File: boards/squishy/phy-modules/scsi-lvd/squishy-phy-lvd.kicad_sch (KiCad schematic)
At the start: 14 parts, among them J1 SCSI PHY Mezz, J2 SCSI Connector, U1 M24C02-RMC

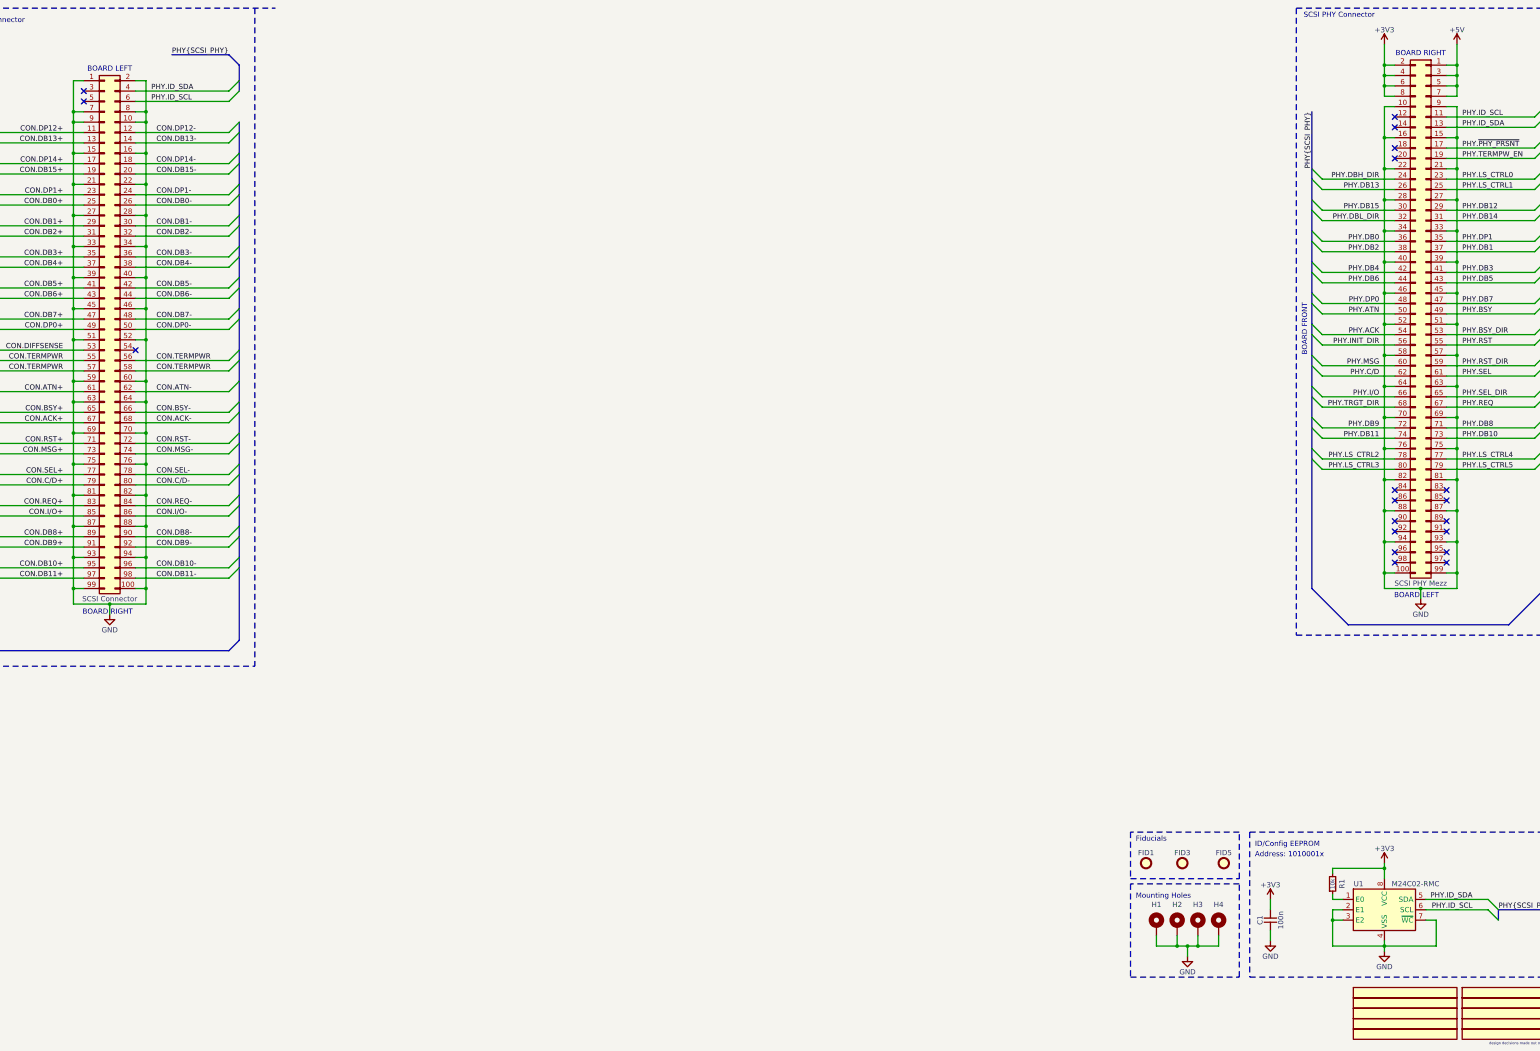
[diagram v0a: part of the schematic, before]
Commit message: squishy: phy: lvd: Large chunk of work on the LVD phy,
still needs diffsense and termpwr bits implemented and then it can be routed
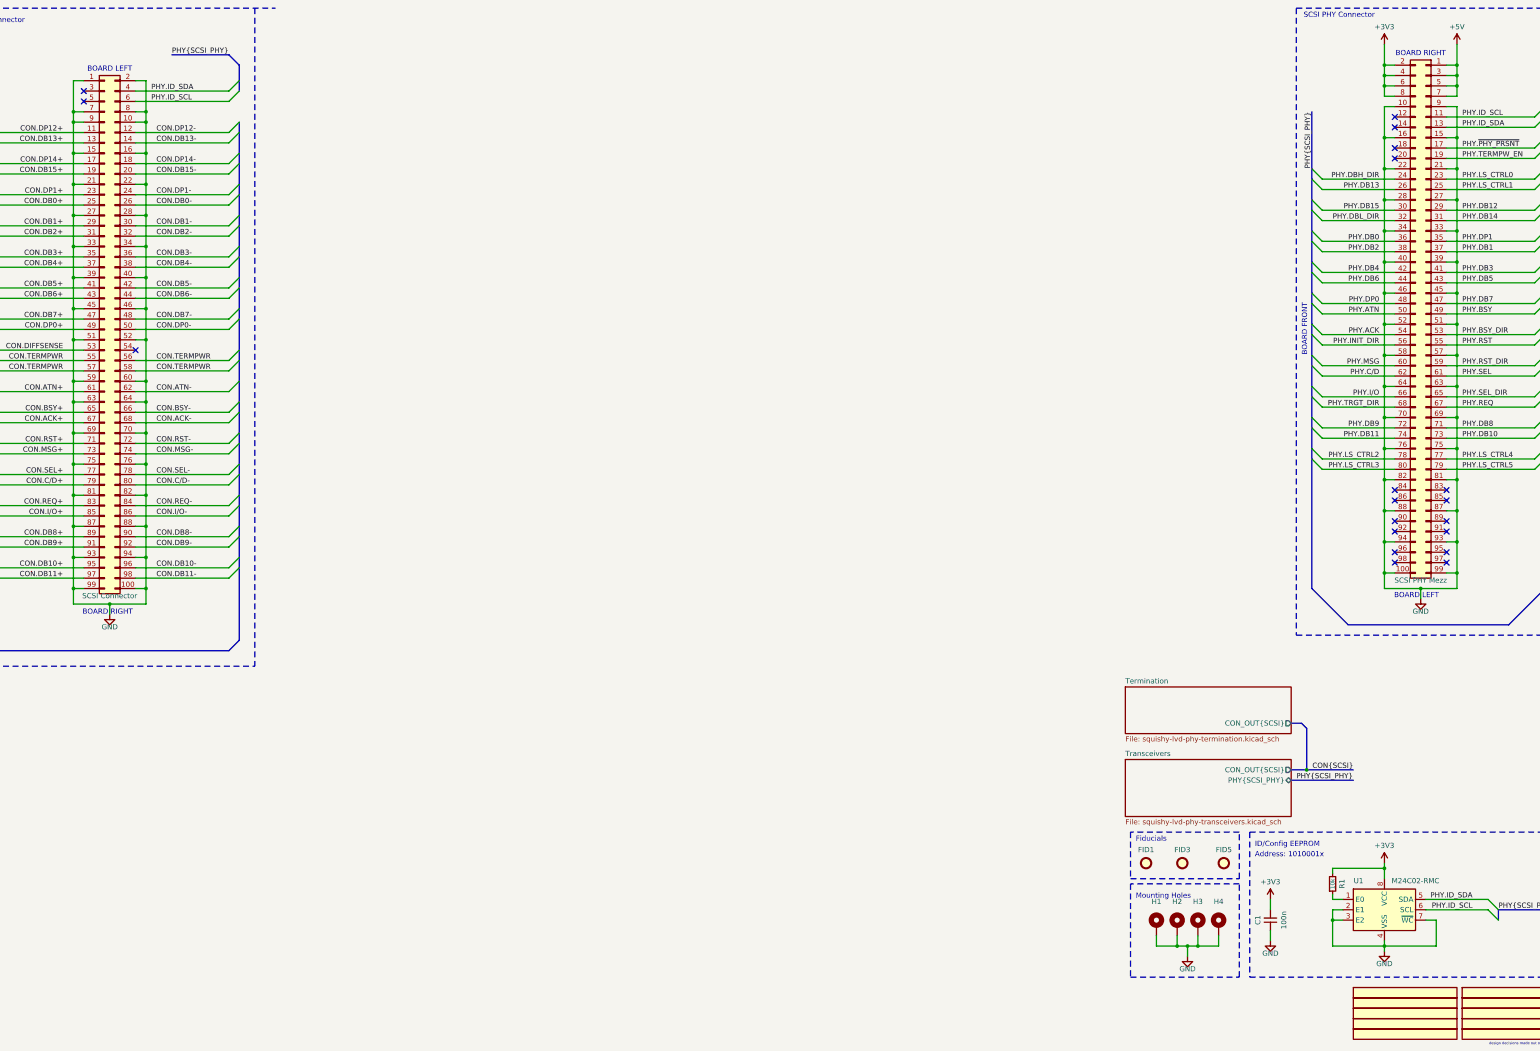
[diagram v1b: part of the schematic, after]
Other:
- added sheet Termination (squishy-lvd-phy-termination.kicad_sch)
- added sheet Transceivers (squishy-lvd-phy-transceivers.kicad_sch)

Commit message: squishy: phy: updated the pinout to the connector module to allow for +3v3 so we can power the ID chip on the board
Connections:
- net +3V3: now also J2.3 (Pin_3)
- no-connect marks 19 -> 18

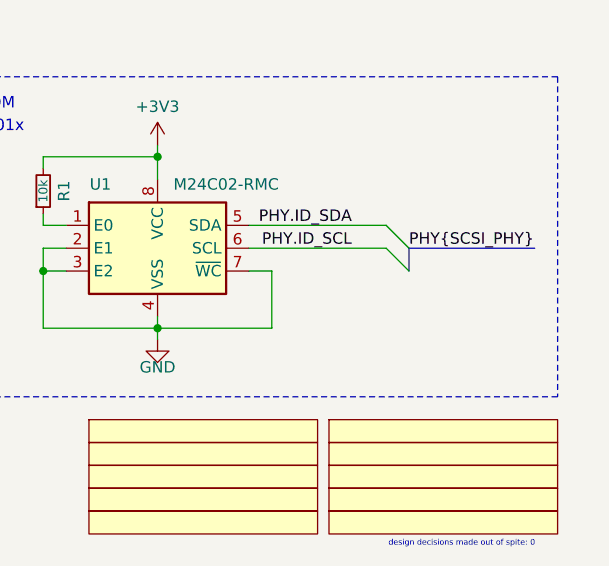
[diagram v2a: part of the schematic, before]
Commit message: squishy: phy: Added debug/programming connector for the PHY EEPROMs
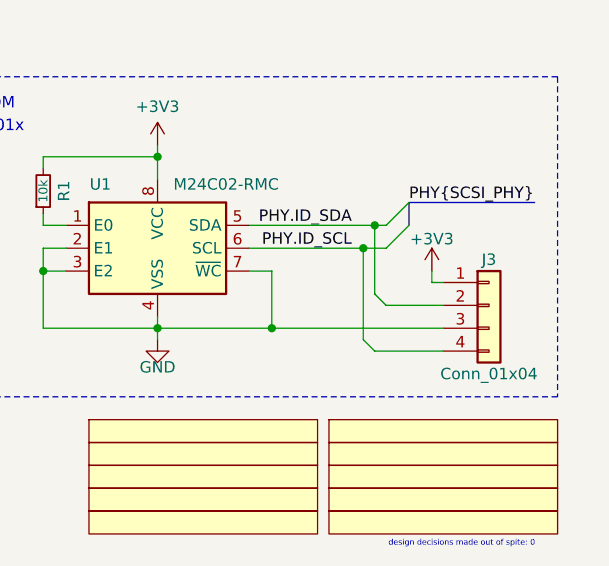
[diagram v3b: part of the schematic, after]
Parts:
- added J3: Conn_01x04, pkl_connectors_wuerth:490107670412-d, symbol Connector_Generic:Conn_01x04
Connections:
- net +3V3: now also J3.1 (Pin_1)
- net GND: now also J3.3 (Pin_3)
- net PHY.ID_SCL: now also J3.4 (Pin_4)
- net PHY.ID_SDA: now also J3.2 (Pin_2)

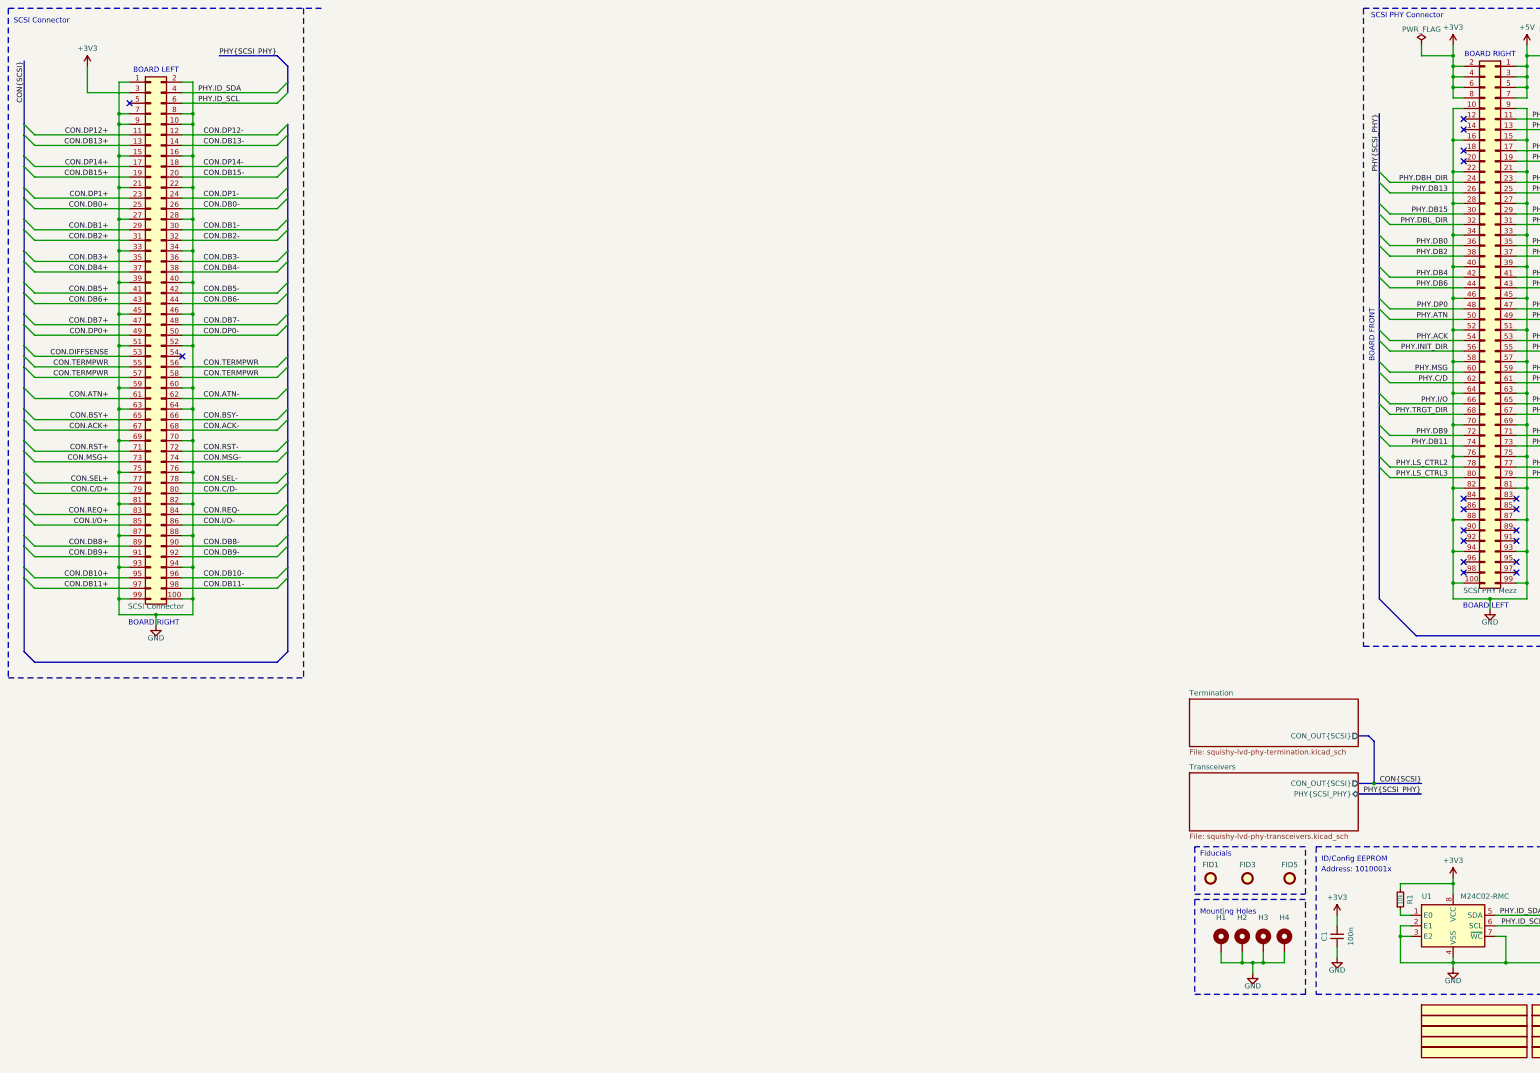
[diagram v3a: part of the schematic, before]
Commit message: squishy: phy: added `DIFFSENS` discriminator to the LVD PHY
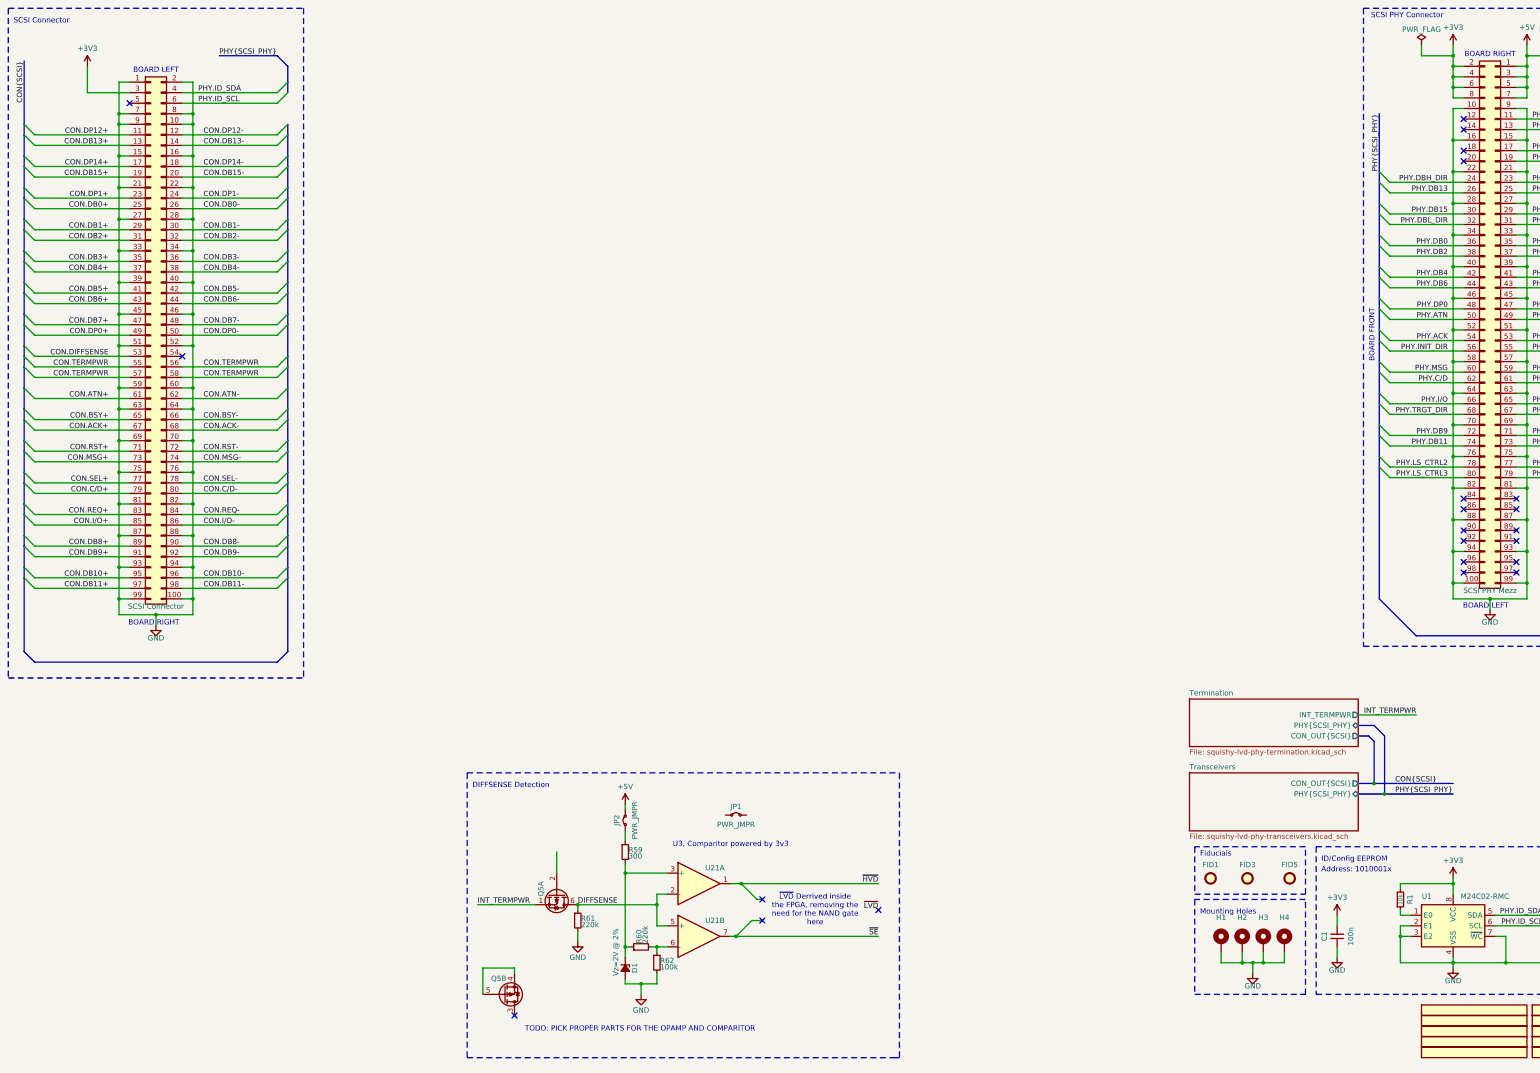
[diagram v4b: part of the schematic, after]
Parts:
- added D1: Vz=2V @ 2%, symbol Device:D_Zener_Small_Filled
- added JP1, JP2: PWR_JMPR, pkl_jumpers:J_NC_0402_30, symbol Jumper:Jumper_2_Small_Bridged
- added Q5: PMDPB58UPE,115, lethalbit-so:SOT1118-3, symbol Device:Q_Dual_PMOS_S1G1D2S2G2D1
- added R59: 300, symbol Device:R_Small
- added R60, R61: 220k, symbol Device:R_Small
- added R62: 100k, symbol Device:R_Small
- added U21: MCP6562, symbol Comparator:MCP6562
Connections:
- net +5V: now also JP2.2 (B)
- net GND: now also D1.2 (A), R61.2, R62.2
- new net: JP2.1 (A), R59.1
- new net: D1.1 (K), R59.2, R60.1, U21.3 (+)
- new net: R60.2, R62.1, U21.6 (-)
- new net: Q5.4 (S), Q5.5 (G)
- new net DIFFSENSE: Q5.6 (D), R61.1, U21.2 (-), U21.5 (+)
- new net INT_TERMPWR: Q5.1 (S)
- new net ~{HVD}: U21.1
- new net ~{SE}: U21.7
- no-connect marks 18 -> 22
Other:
- sheet Termination ports: added INT_TERMPWR, PHY{SCSI_PHY}; removed none
- note added: "DIFFSENSE Detection"
- note added: "TODO: PICK PROPER PARTS FOR THE OPAMP AND COMPARITOR"
- note added: "U3, Comparitor powered by 3v3"
- note added: "~{LVD} Derrived inside the FPGA, removing the need for the NAND gate here"

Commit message: squishy: phy: lvd: Fixed up the DIFFSENSE detection and sourcing, as well as added TERMWPR control
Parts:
- removed U21: MCP6562, symbol Comparator:MCP6562
- added C81, C86: 100n, rhais_rcl:C0603, symbol Device:C_Small
- added JP3, JP4: PWR_JMPR, pkl_jumpers:J_NC_0402_30, symbol Jumper:Jumper_2_Small_Bridged
- added Q6: DMN65D8L-7, Package_TO_SOT_SMD:SOT-23, symbol Device:Q_NMOS_GSD
- added R63, R64, R67, R68, R69, R70, R71: 10k, rhais_rcl:R0603, symbol Device:R_Small
- added R65: 100k, rhais_rcl:R0402, symbol Device:R_Small
- added R66: 175k, rhais_rcl:R0402, symbol Device:R_Small
- added U21: LM321, Package_TO_SOT_SMD:SOT-23-5, symbol Amplifier_Operational:LM321
- added U39: LM2903, Package_SON:WSON-8-1EP_2x2mm_P0.5mm_EP0.9x1.6mm, symbol Comparator:LM2903
- D1: footprint (none) -> Diode_SMD:D_SOD-323
- R59, R60, R61, R62: footprint (none) -> rhais_rcl:R0402
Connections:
- net DIFFSENSE is gone; now on net CON.DIFFSENSE: Q5.6 (D), R61.1
- net +3V3: now also JP3.2 (B), R63.2, R64.2, R67.2, R69.1
- net +5V: now also JP1.2 (B), Q5.4 (S), C86.2, JP4.2 (B), R71.1
- net CON.DIFFSENSE: now also U39.2 (-), U39.5 (+)
- net CON.TERMPWR: now also Q5.3 (D)
- net GND: now also C81.1, C86.1, Q6.2 (S), U21.2 (V-), U39.4 (V-)
- net INT_TERMPWR: no longer Q5.1 (S)
- net PHY.LS_CTRL4: now also Q5.2 (G), R67.1
- net PHY.TERMPW_EN: now also R68.1, R69.2
- net ~{HVD}: now also R64.1, U39.1
- net ~{SE}: now also R63.1, U39.7
- net at D1.1 (K), R59.2, R60.1: now also U39.3 (+)
- net at R60.2, R62.1: now also U39.6 (-)
- net at JP1.1 (A): now also C81.2, U39.8 (V+)
- net at Q5.5 (G): now also R70.2; no longer Q5.4 (S)
- new net: JP3.1 (A), R66.1
- new net: R65.1, R66.2, U21.1 (+)
- new net: Q6.1 (G), R68.2
- new net: Q6.3 (D), R70.1, R71.2
- new net: JP4.1 (A), U21.5 (V+)
- new net: Q5.1 (S), R65.2, U21.3 (-), U21.4
- no-connect marks 22 -> 18
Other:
- note added: "0.5V"
- note added: "0.7V"
- note added: "0V"
- note added: "1.2V"
- note added: "1.9V"
- note added: "2.4V"
- note added: "2V"
- note added: "5V"
- note added: "625mV"
- note added: "DIFFSENSE"
- note added: "DIFFSENSE LEVELS"
- note added: "HVD"
- note added: "IND"
- note added: "LS_CTRL0 -> Emphases Enabled LS_CTRL1 -> High Bits Enabled (DB8-DB15) LS_CTRL4 -> Provide DIFFSENSE LS_CTRL5 -> LVD Termination Enable"
- note added: "LVD"
- note added: "MAX"
- note added: "MIN"
- note added: "SE"
- note added: "SEE: T10/1525D Pg 92 §7.2 Table 29"
- note added: "TERMPWR Enable"
- note removed: "DIFFSENSE Detection"
- note removed: "TODO: PICK PROPER PARTS FOR THE OPAMP AND COMPARITOR"
- note removed: "U3, Comparitor powered by 3v3"
- moved on the sheet: D1, JP1, JP2, Q5A, Q5B, R59, R60, R61, R62

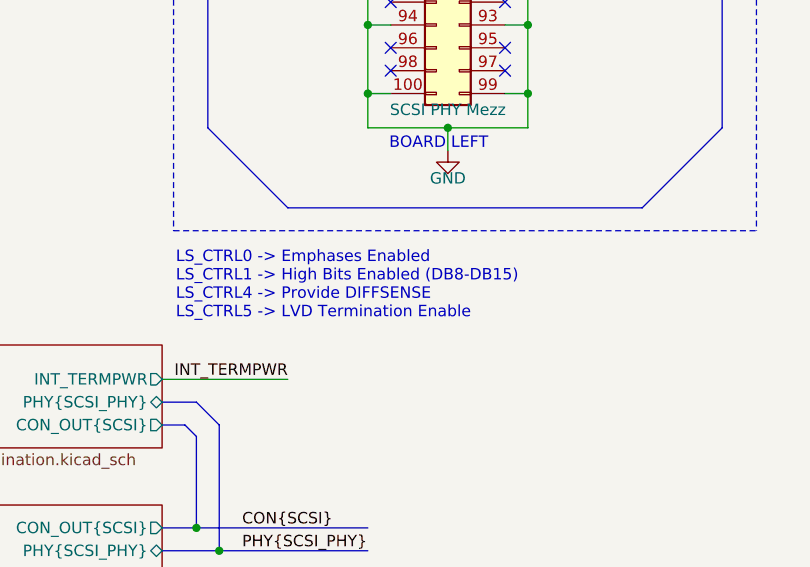
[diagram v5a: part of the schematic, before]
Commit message: squishy: phy: lvd: updated the PCB with the mostly finished schematic bits.
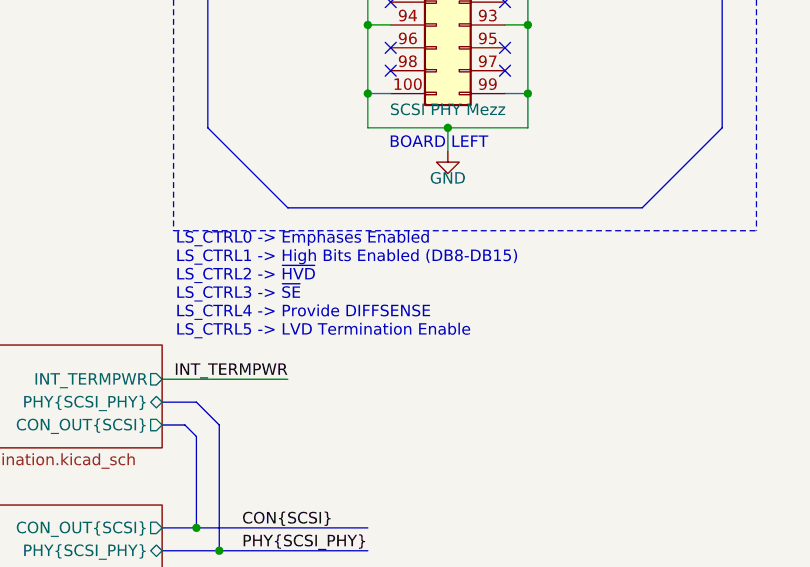
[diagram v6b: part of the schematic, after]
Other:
- note added: "LS_CTRL0 -> Emphases Enabled LS_CTRL1 -> High Bits Enabled (DB8-DB15) LS_CTRL2 -> ~{HVD} LS_CTRL3 -> ~{SE} LS_CTRL4 -> Provide DIFFSENSE LS_CTRL5 -> LVD Termination Enable"
- note removed: "LS_CTRL0 -> Emphases Enabled LS_CTRL1 -> High Bits Enabled (DB8-DB15) LS_CTRL4 -> Provide DIFFSENSE LS_CTRL5 -> LVD Termination Enable"
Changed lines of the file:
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@@
 		)
 	)
-	(text "LS_CTRL0 -> Emphases Enabled\nLS_CTRL1 -> High Bits Enabled (DB8-DB15)\nLS_CTRL4 -> Provide DIFFSENSE\nLS_CTRL5 -> LVD Termination Enable"
+	(text "LS_CTRL0 -> Emphases Enabled\nLS_CTRL1 -> High Bits Enabled (DB8-DB15)\nLS_CTRL2 -> ~{HVD}\nLS_CTRL3 -> ~{SE}\nLS_CTRL4 -> Provide DIFFSENSE\nLS_CTRL5 -> LVD Termination Enable"
 		(exclude_from_sim no)
 		(at 340.614 173.736 0)
@@
 	(label "CON.TERMPWR"
 		(at 74.93 246.38 180)
+		(fields_autoplaced yes)
 		(effects
 			(font
@@
 	(label "CON.DIFFSENSE"
 		(at 127 242.57 270)
+		(fields_autoplaced yes)
 		(effects
 			(font
@@
 	(label "PHY.LS_CTRL4"
 		(at 119.38 232.41 90)
+		(fields_autoplaced yes)
 		(effects
 			(font
@@
 	(label "PHY.TERMPW_EN"
 		(at 19.05 267.97 0)
-		(effects
-			(font
+		(fields_autoplaced yes)
+		(effects
+			(font
